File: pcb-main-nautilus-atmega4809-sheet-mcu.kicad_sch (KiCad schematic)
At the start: 20 parts, among them SW1 PTS645SH43SMTR92 LFS, U4 ATmega4809-A

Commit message: Fix NetTie usage
Supports #2.
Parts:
- NT2, NT3: now in the parts list
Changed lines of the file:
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@@
   )
   (symbol (lib_id "Device:NetTie_3") (at 182.88 69.85 0) (unit 1)
-    (in_bom no) (on_board yes) (fields_autoplaced)
+    (in_bom yes) (on_board yes) (fields_autoplaced)
     (property "Reference" "NT2" (id 0) (at 182.88 64.77 0))
     (property "Value" "NetTie_3" (id 1) (at 182.88 67.31 0))
@@
   )
   (symbol (lib_id "Device:NetTie_3") (at 182.88 82.55 0) (unit 1)
-    (in_bom no) (on_board yes) (fields_autoplaced)
+    (in_bom yes) (on_board yes) (fields_autoplaced)
     (property "Reference" "NT3" (id 0) (at 182.88 77.47 0))
     (property "Value" "NetTie_3" (id 1) (at 182.88 80.01 0))

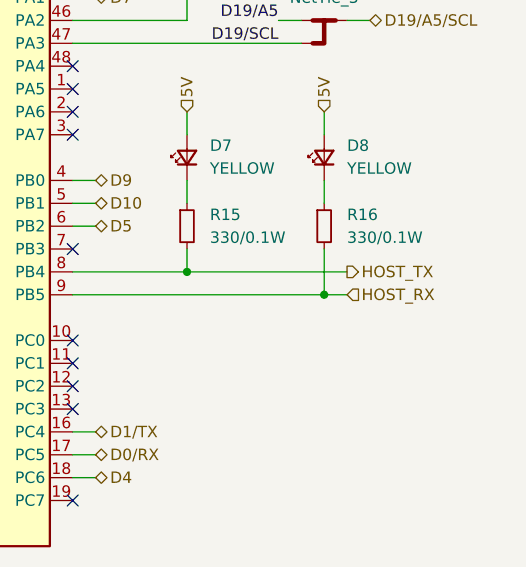
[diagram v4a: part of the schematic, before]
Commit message: Rename serial signals
Supports #2.
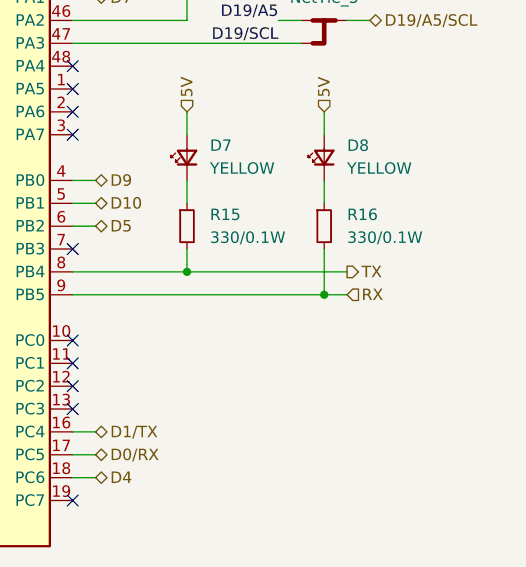
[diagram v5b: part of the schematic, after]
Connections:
- net HOST_RX renamed RX
- net HOST_TX renamed TX
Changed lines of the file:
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@@
     (effects (font (size 1.27 1.27)) (justify right))
   )
-  (hierarchical_label "HOST_RX" (shape input) (at 185.42 113.03 0)
+  (hierarchical_label "RX" (shape input) (at 185.42 113.03 0)
     (effects (font (size 1.27 1.27)) (justify left))
   )
@@
     (effects (font (size 1.27 1.27)) (justify left))
   )
-  (hierarchical_label "HOST_TX" (shape output) (at 185.42 110.49 0)
+  (hierarchical_label "TX" (shape output) (at 185.42 110.49 0)
     (effects (font (size 1.27 1.27)) (justify left))
   )

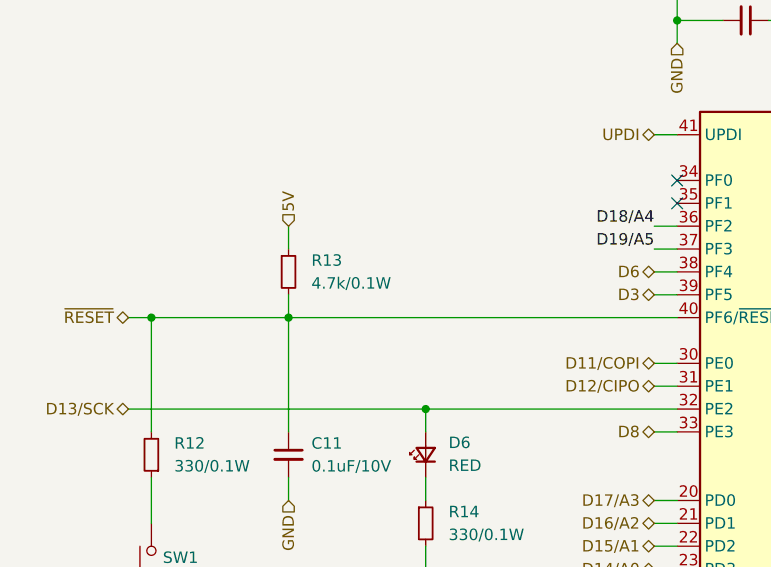
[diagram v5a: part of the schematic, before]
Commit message: Reduce ~{RESET} pull-up strength
Supports #2.
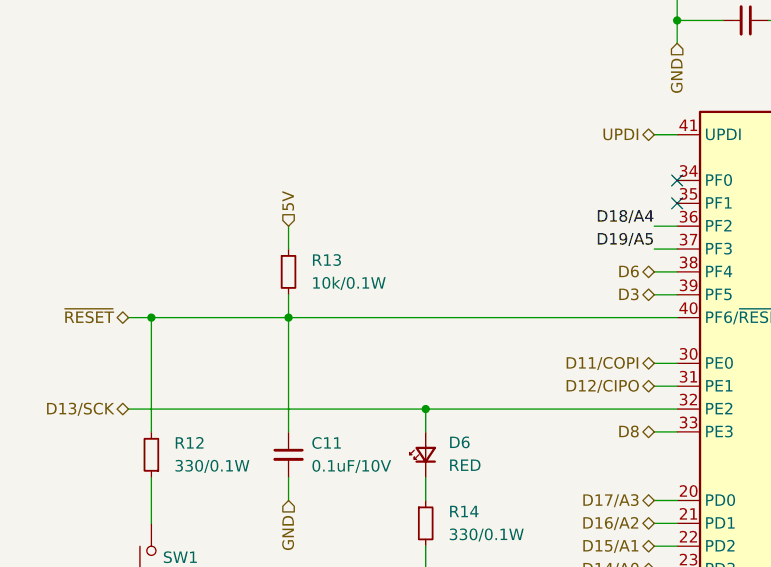
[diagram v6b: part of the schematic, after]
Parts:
- R13: value 4.7k/0.1W -> 10k/0.1W; Digi-Key Part Number P4.70KHCT-ND -> P10.0KHCT-ND; Manufacturer Part Number ERJ-3EKF4701V -> ERJ-3EKF1002V; Mouser Part Number 667-ERJ-3EKF4701V -> 667-ERJ-3EKF1002V
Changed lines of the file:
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@@
       (effects (font (size 1.27 1.27)) (justify left))
     )
-    (property "Value" "4.7k/0.1W" (id 1) (at 83.82 93.9799 0)
+    (property "Value" "10k/0.1W" (id 1) (at 83.82 93.9799 0)
       (effects (font (size 1.27 1.27)) (justify left))
     )
@@
       (effects (font (size 1.27 1.27)) hide)
     )
-    (property "Manufacturer Part Number" "ERJ-3EKF4701V" (id 5) (at 81.28 92.71 0)
+    (property "Manufacturer Part Number" "ERJ-3EKF1002V" (id 5) (at 81.28 92.71 0)
       (effects (font (size 1.27 1.27)) hide)
     )
-    (property "Digi-Key Part Number" "P4.70KHCT-ND" (id 6) (at 81.28 92.71 0)
+    (property "Digi-Key Part Number" "P10.0KHCT-ND" (id 6) (at 81.28 92.71 0)
       (effects (font (size 1.27 1.27)) hide)
     )
-    (property "Mouser Part Number" "667-ERJ-3EKF4701V" (id 7) (at 81.28 92.71 0)
+    (property "Mouser Part Number" "667-ERJ-3EKF1002V" (id 7) (at 81.28 92.71 0)
       (effects (font (size 1.27 1.27)) hide)
     )

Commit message: Update BOM
Supports #2.
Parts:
- C12, C14, C17: Mouser Part Number 80-C0603C106M9PAC -> 80-C0603C475M8PACLR
- R12, R14, R15, R16: Manufacturer Part Number ERJ-3EKF3300V -> ERJ-3EKF3300
- R13: Manufacturer Part Number ERJ-3EKF1002V -> ERJ-3EKF1002
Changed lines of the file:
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@@
       (effects (font (size 1.27 1.27)) hide)
     )
-    (property "Manufacturer Part Number" "ERJ-3EKF3300V" (id 5) (at 96.52 120.65 0)
+    (property "Manufacturer Part Number" "ERJ-3EKF3300" (id 5) (at 96.52 120.65 0)
       (effects (font (size 1.27 1.27)) hide)
     )
@@
       (effects (font (size 1.27 1.27) italic) hide)
     )
-    (property "Datasheet" "http://ww1.microchip.com/downloads/en/DeviceDoc/40002016A.pdf" (id 3) (at 139.7 107.95 0)
+    (property "Datasheet" "https://ww1.microchip.com/downloads/aemDocuments/documents/MCU08/ProductDocuments/DataSheets/ATmega4808-09-DataSheet-DS40002173C.pdf" (id 3) (at 139.7 107.95 0)
       (effects (font (size 1.27 1.27)) hide)
     )
@@
       (effects (font (size 1.27 1.27)) hide)
     )
-    (property "Manufacturer Part Number" "ERJ-3EKF3300V" (id 5) (at 66.04 113.03 0)
+    (property "Manufacturer Part Number" "ERJ-3EKF3300" (id 5) (at 66.04 113.03 0)
       (effects (font (size 1.27 1.27)) hide)
     )
@@
       (effects (font (size 1.27 1.27)) hide)
     )
-    (property "Datasheet" "https://connect.kemet.com:7667/gateway/IntelliData-ComponentDocumentation/1.0/download/datasheet/C0603C104M8RACTU" (id 3) (at 96.52 140.97 0)
+    (property "Datasheet" "https://connect.kemet.com:7667/gateway/IntelliData-ComponentDocumentation/1.0/download/datasheet/C0603C475M8PACTU" (id 3) (at 96.52 140.97 0)
       (effects (font (size 1.27 1.27)) hide)
     )
@@
       (effects (font (size 1.27 1.27)) hide)
     )
-    (property "Mouser Part Number" "80-C0603C106M9PAC" (id 7) (at 96.52 140.97 0)
+    (property "Mouser Part Number" "80-C0603C475M8PACLR" (id 7) (at 96.52 140.97 0)
       (effects (font (size 1.27 1.27)) hide)
     )
@@
       (effects (font (size 1.27 1.27)) hide)
     )
-    (property "Manufacturer Part Number" "ERJ-3EKF3300V" (id 5) (at 167.64 105.41 0)
+    (property "Manufacturer Part Number" "ERJ-3EKF3300" (id 5) (at 167.64 105.41 0)
       (effects (font (size 1.27 1.27)) hide)
     )
@@
       (effects (font (size 1.27 1.27)) hide)
     )
-    (property "Datasheet" "https://connect.kemet.com:7667/gateway/IntelliData-ComponentDocumentation/1.0/download/datasheet/C0603C104M8RACTU" (id 3) (at 132.08 44.45 0)
+    (property "Datasheet" "https://connect.kemet.com:7667/gateway/IntelliData-ComponentDocumentation/1.0/download/datasheet/C0603C475M8PACTU" (id 3) (at 132.08 44.45 0)
       (effects (font (size 1.27 1.27)) hide)
     )
@@
       (effects (font (size 1.27 1.27)) hide)
     )
-    (property "Mouser Part Number" "80-C0603C106M9PAC" (id 7) (at 132.08 44.45 0)
+    (property "Mouser Part Number" "80-C0603C475M8PACLR" (id 7) (at 132.08 44.45 0)
       (effects (font (size 1.27 1.27)) hide)
     )
@@
       (effects (font (size 1.27 1.27)) hide)
     )
-    (property "Manufacturer Part Number" "ERJ-3EKF3300V" (id 5) (at 182.88 105.41 0)
+    (property "Manufacturer Part Number" "ERJ-3EKF3300" (id 5) (at 182.88 105.41 0)
       (effects (font (size 1.27 1.27)) hide)
     )
@@
       (effects (font (size 1.27 1.27)) hide)
     )
-    (property "Datasheet" "https://connect.kemet.com:7667/gateway/IntelliData-ComponentDocumentation/1.0/download/datasheet/C0603C104M8RACTU" (id 3) (at 149.86 54.61 0)
+    (property "Datasheet" "https://connect.kemet.com:7667/gateway/IntelliData-ComponentDocumentation/1.0/download/datasheet/C0603C475M8PACTU" (id 3) (at 149.86 54.61 0)
       (effects (font (size 1.27 1.27)) hide)
     )
@@
       (effects (font (size 1.27 1.27)) hide)
     )
-    (property "Mouser Part Number" "80-C0603C106M9PAC" (id 7) (at 149.86 54.61 0)
+    (property "Mouser Part Number" "80-C0603C475M8PACLR" (id 7) (at 149.86 54.61 0)
       (effects (font (size 1.27 1.27)) hide)
     )
@@
       (effects (font (size 1.27 1.27)) hide)
     )
-    (property "Manufacturer Part Number" "ERJ-3EKF1002V" (id 5) (at 81.28 92.71 0)
-      (effects (font (size 1.27 1.27)) hide)
-    )
+    (property "Manufacturer Part Number" "ERJ-3EKF1002" (id 5) (at 81.28 92.71 0)
+      (effects (font (size 1.27 1.27)) hide)
+    )

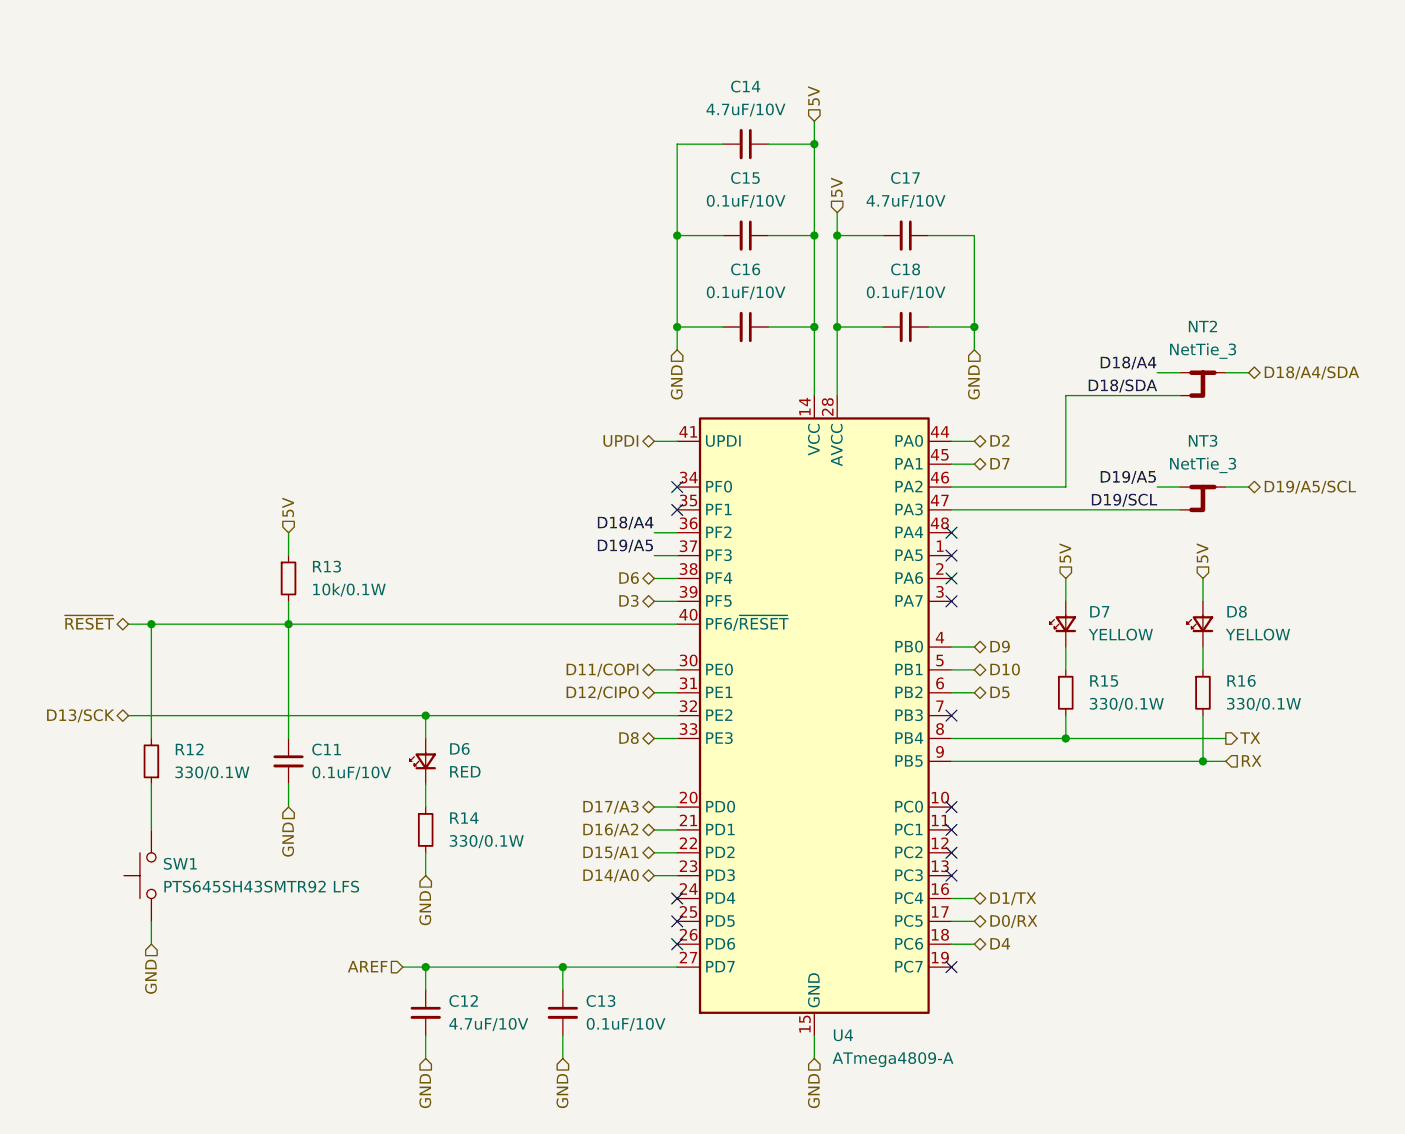
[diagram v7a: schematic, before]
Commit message: Remove improperly used netties
Supports #2.
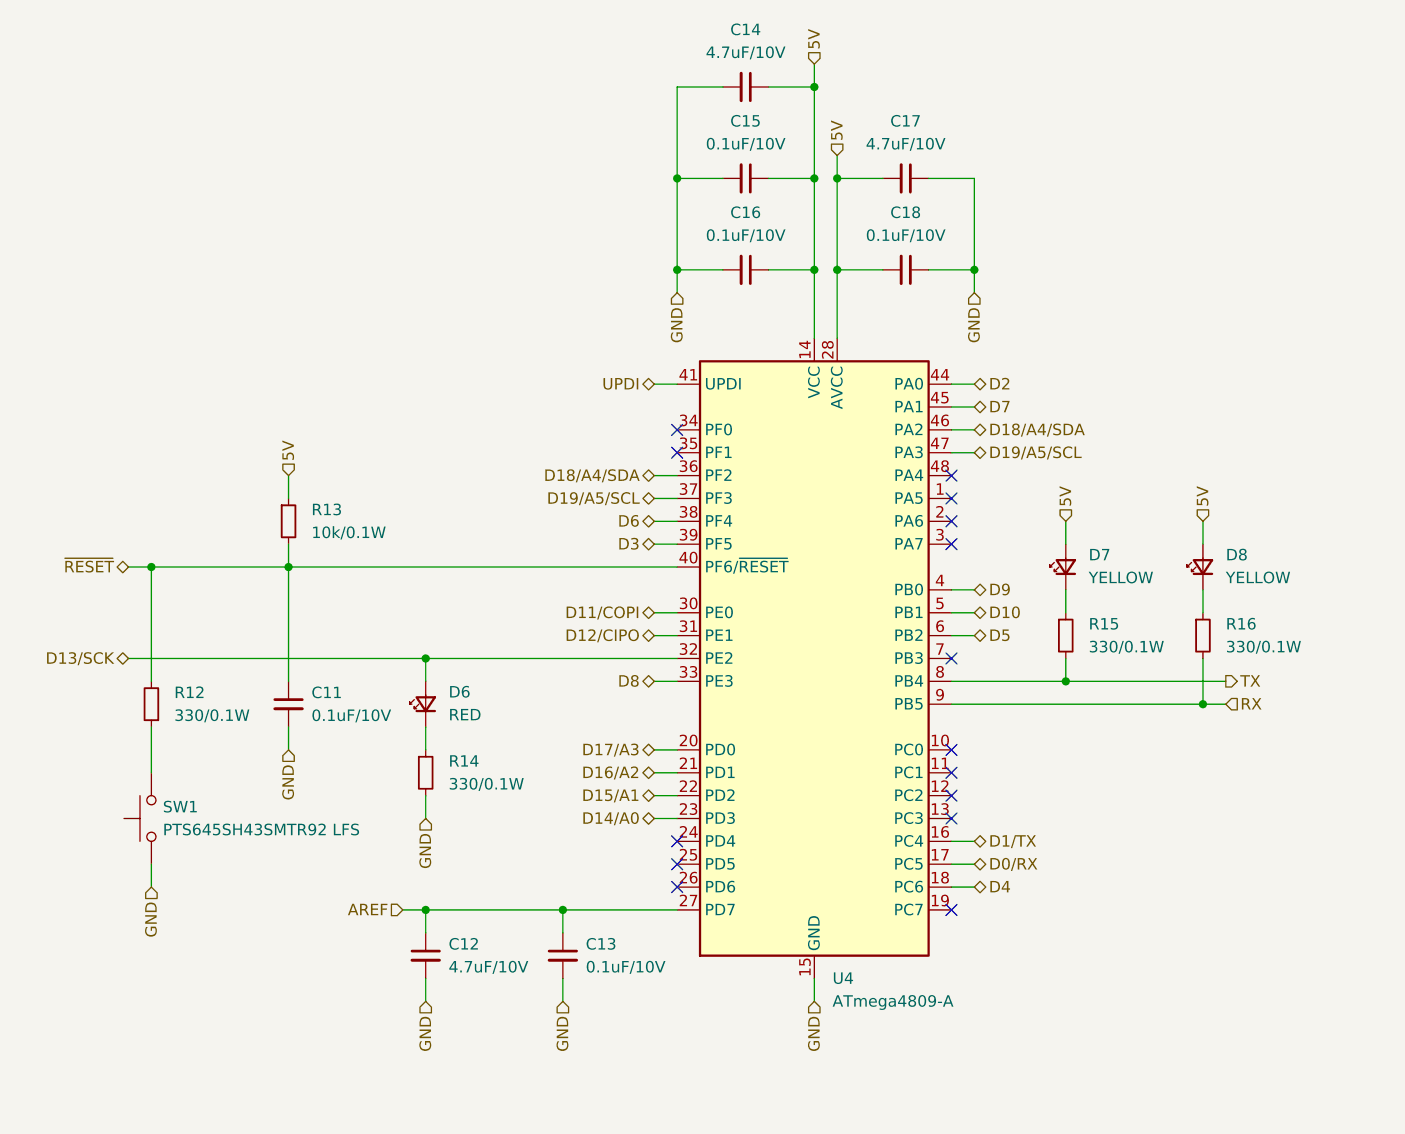
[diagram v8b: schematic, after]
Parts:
- removed NT2, NT3: NetTie_3, NetTie:NetTie-3_SMD_Pad0.5mm, symbol Device:NetTie_3
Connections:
- net D18/A4 is gone; now on net D18/A4/SDA: U4.36 (PF2)
- net D18/SDA is gone; now on net D18/A4/SDA: U4.46 (PA2)
- net D19/A5 is gone; now on net D19/A5/SCL: U4.37 (PF3)
- net D19/SCL is gone; now on net D19/A5/SCL: U4.47 (PA3)
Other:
- moved on the sheet: C11, C12, C13, C14, C15, C16, C17, C18, D6, D7, D8, R12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
